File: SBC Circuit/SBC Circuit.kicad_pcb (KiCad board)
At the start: 2 copper layers, 127 x 114.3 mm, 82 parts, among them J1 USB_B, J2 Conn_01x02_Pin, J3 Conn_01x06_Pin, J4 Conn_01x06_Pin, J5 Conn_01x03_Pin, J6 Conn_01x08_Pin, J7 Conn_01x06_Pin, J8 Conn_01x02_Pin, J9 Conn_02x04_Odd_Even, Q1 AOI21357, Q2 AOI21357, SW1 RESET, U1 MC68000FN, U10 FT230XS, U11 MC34064P, U2 XC9572XL, U3 68681, U4 MCM6206CP, U5 MCM6206CP, U6 28C256, U7 28C256, U8 LM7805_TO220, U9 LD1117AV33, X1 SG-531, X2 EC11

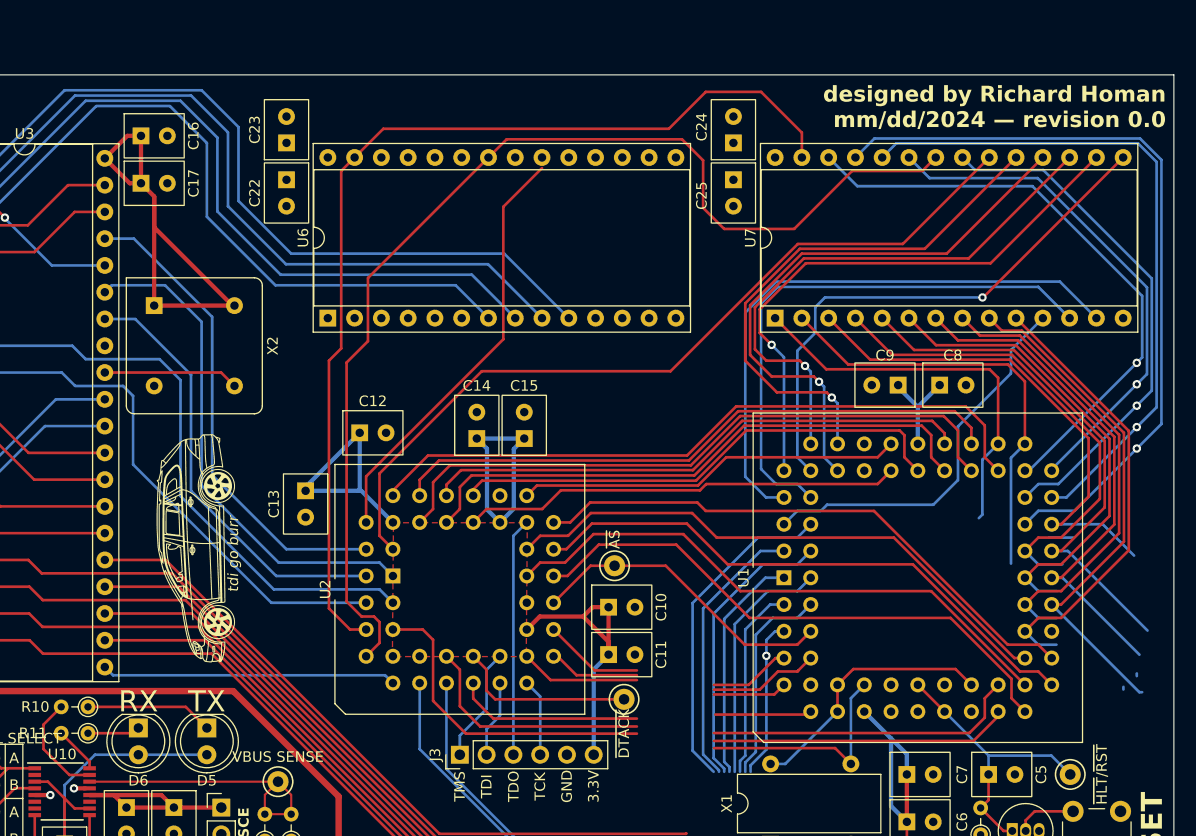
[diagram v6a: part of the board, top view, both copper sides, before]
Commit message: Wire ROM low
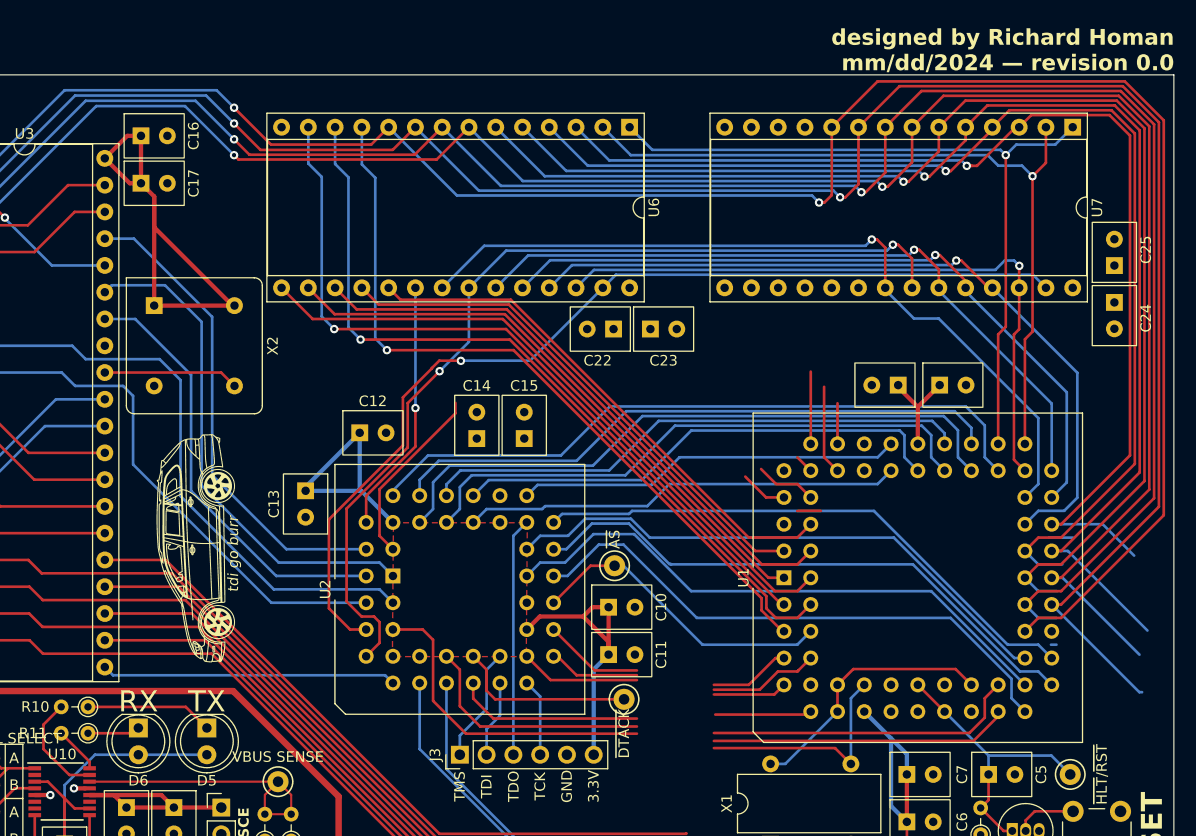
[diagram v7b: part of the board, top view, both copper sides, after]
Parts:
- moved C24 39.2 mm to (197.5, 55.0), turned to -90 degrees
- moved C23 38.8 mm to (153.5, 57.5), turned to 0 degrees
- moved C25 37.0 mm to (197.5, 51.5), turned to 90 degrees
- moved C22 34.1 mm to (150.0, 57.5), turned to 180 degrees
- moved U6 33.9 mm to (151.5, 38.3), turned to -90 degrees
- moved U7 33.5 mm to (193.6, 38.3), turned to -90 degrees
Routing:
- net addr4: track 45.4 -> 121.5 mm, vias 0 -> 1
- net addr1: track 123.1 -> 197.1 mm, vias 0 -> 2
- net addr2: track 118.9 -> 191.6 mm, vias 0 -> 2
- net addr0: track 118.0 -> 190.0 mm, vias 0 -> 2
- net addr3: track 122.6 -> 194.5 mm, vias 0 -> 2
- net addr5: track 51.2 -> 121.1 mm, vias 0 -> 1
- net addr6: track 46.6 -> 110.0 mm, vias 0 -> 1
- net romh_cs: track 78.0 -> 17.4 mm
- net addr7: track 48.6 -> 106.9 mm, vias 0 -> 1
- net data0: track 81.1 -> 137.5 mm
- net data1: track 94.7 -> 150.9 mm, vias 0 -> 1
- net data2: track 82.1 -> 137.5 mm, vias 0 -> 1
- net data12: track 54.2 -> 0.00 mm, vias 1 -> 0
- net data10: track 56.0 -> 4.49 mm
- net data11: track 51.9 -> 1.80 mm, vias 1 -> 0
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
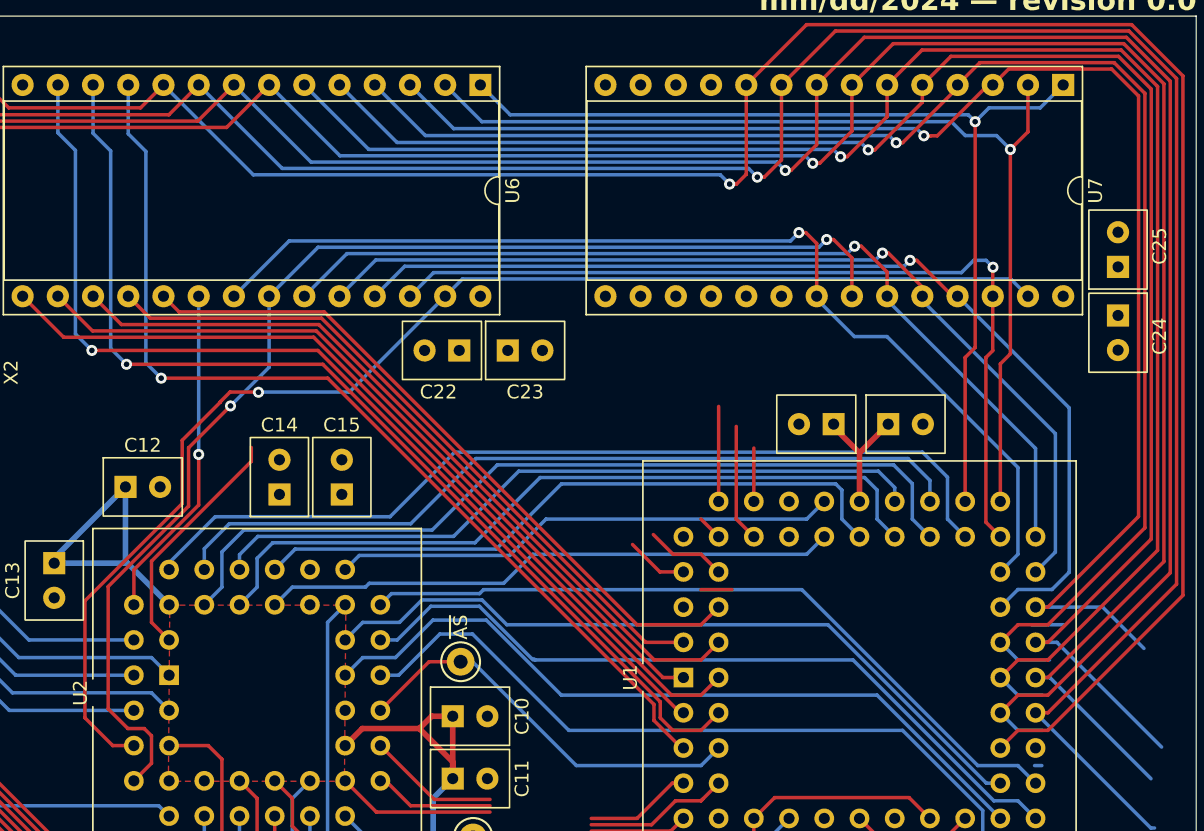
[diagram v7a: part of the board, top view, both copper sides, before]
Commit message: Finished wiring ROM High
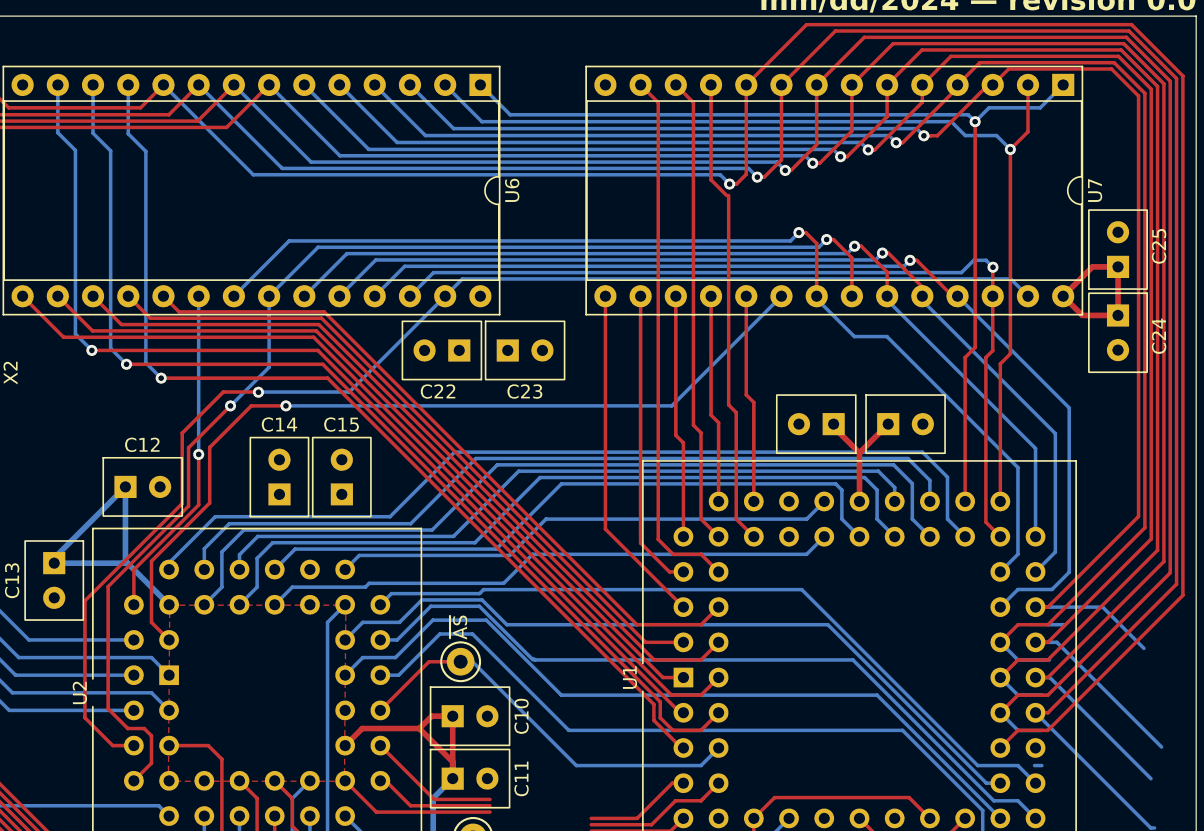
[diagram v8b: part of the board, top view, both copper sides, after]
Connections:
- U7 pad 11: data8 -> data14
- U7 pad 12: data9 -> data11
- U7 pad 13: data10 -> data9
- U7 pad 15: data11 -> data8
- U7 pad 16: data12 -> data10
- U7 pad 17: data13 -> data12
- U7 pad 18: data14 -> data13
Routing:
- net romh_cs: track 17.4 -> 61.9 mm, vias 0 -> 1
- net data9: track 5.83 -> 38.6 mm
- net data11: track 1.80 -> 33.9 mm
- net data14: track 8.48 -> 33.8 mm
- net data8: track 2.24 -> 24.8 mm
- net data12: track 0.00 -> 17.8 mm
- net data10: track 4.49 -> 21.8 mm
- net +5V: track 257.6 -> 270.4 mm
- net data15: track 3.86 -> 15.0 mm
- net data13: track 6.86 -> 15.0 mm
